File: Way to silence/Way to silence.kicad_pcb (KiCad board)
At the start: 2 copper layers, 62 parts, among them J1 SD Card Connector, J2 Amplificator_Terminal, J3 5V_Terminal, J4 Battery_Terminal, Q1 BC817, Q2 BC817, SW1 SW_SPDT, U1 ESP32-WROOM-32-N16, U2 SM5308, U3 CP2102-GMR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

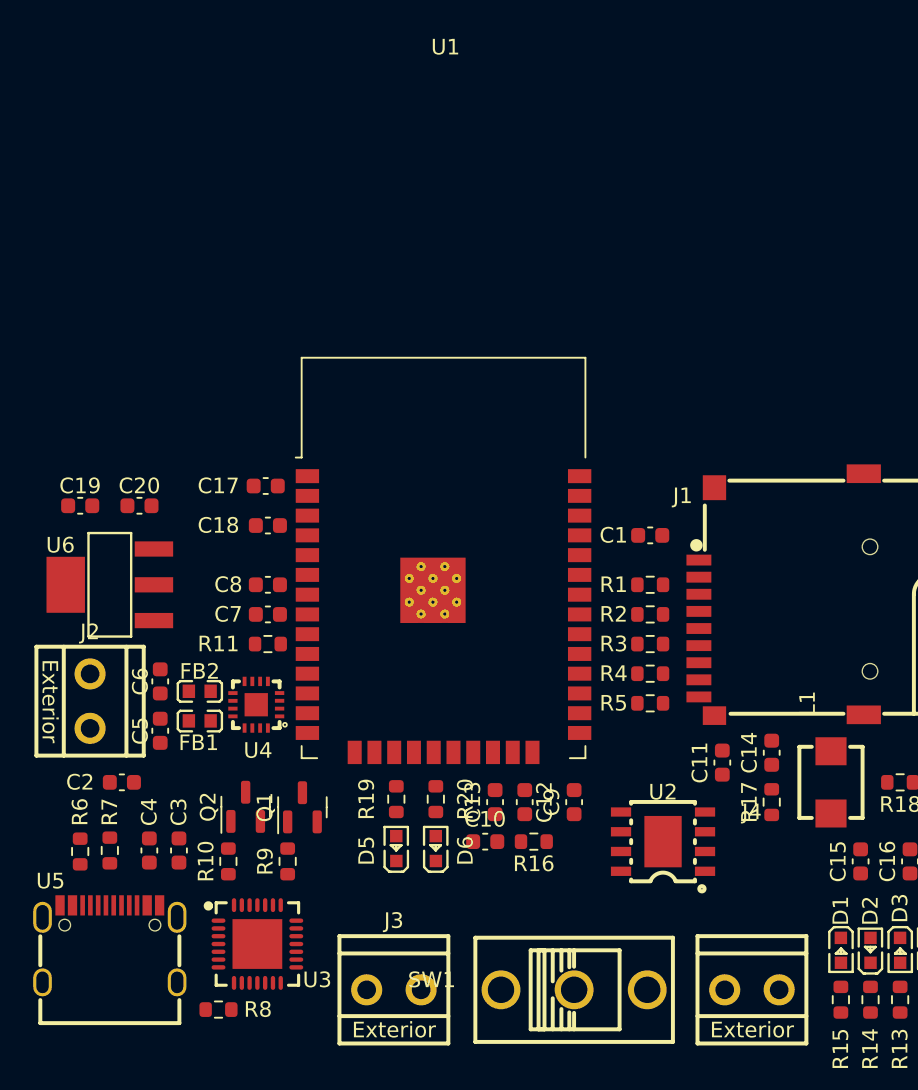
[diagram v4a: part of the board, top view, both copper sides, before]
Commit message: [ADD] Placement adjustements
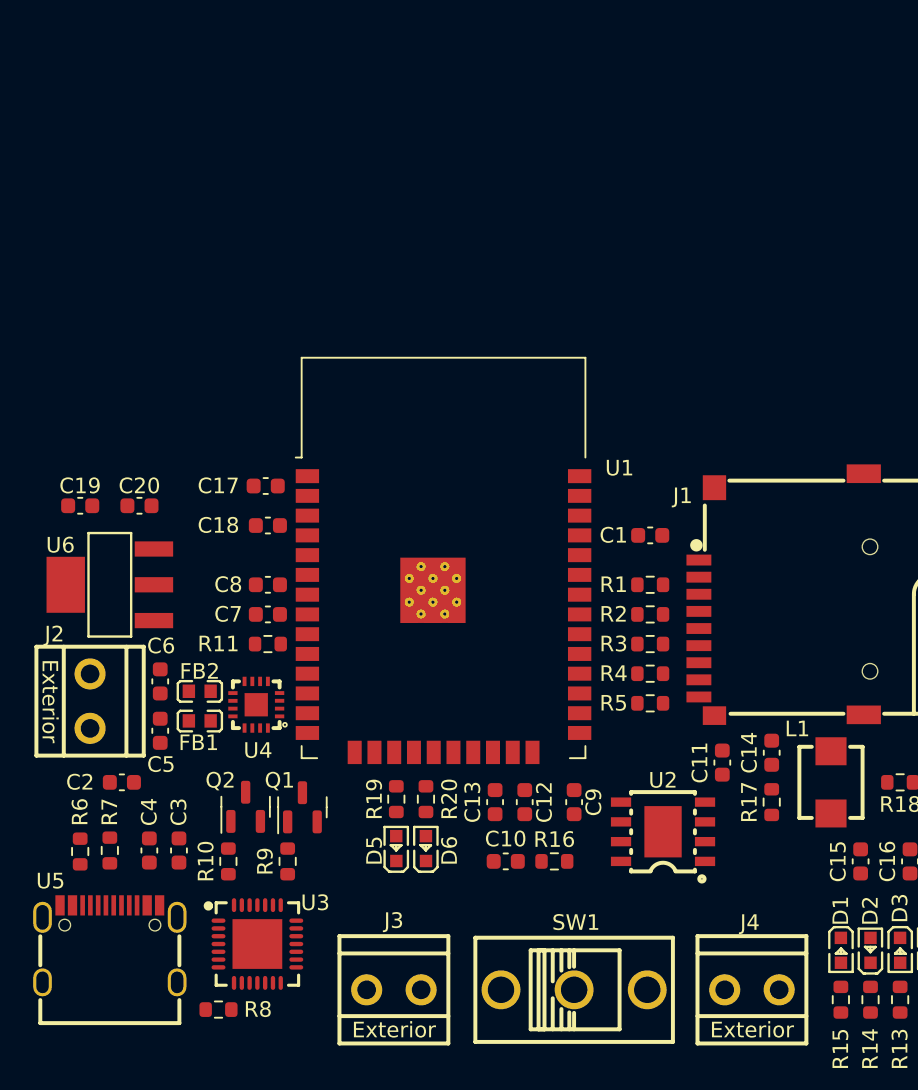
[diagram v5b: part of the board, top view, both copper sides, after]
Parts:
- moved C10 1.83 mm to (94.0, 70.5)
- moved R16 1.83 mm to (97.2, 70.5)
- moved U2 0.64 mm to (104.1, 68.6)
- moved D6 0.63 mm to (88.9, 69.7)
- moved R20 0.63 mm to (88.9, 66.5)
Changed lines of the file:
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@@
     (property "ki_keywords" "screw terminal")
     (attr smd)
-    (fp_text reference "J2" (at -4.445 0 unlocked) (layer "F.SilkS")
+    (fp_text reference "J2" (at -4.305 2.286 unlocked) (layer "F.SilkS")
         (effects (font (size 1 1) (thickness 0.1)))
     )
@@
     (property "ki_keywords" "NPN Transistor")
     (attr smd)
-    (fp_text reference "Q2" (at 0 -2.4 90) (layer "F.SilkS")
+    (fp_text reference "Q2" (at 1.6995 -1.618 180) (layer "F.SilkS")
         (effects (font (size 1 1) (thickness 0.15)))
     )
@@
     (property "ki_keywords" "LED diode")
     (attr smd)
-    (fp_text reference "D5" (at -0.14 -1.905 90 unlocked) (layer "F.SilkS")
+    (fp_text reference "D5" (at -0.14 -1.397 90 unlocked) (layer "F.SilkS")
         (effects (font (size 1 1) (thickness 0.1)))
     )
@@
     (property "ki_keywords" "cap capacitor")
     (attr smd)
-    (fp_text reference "C5" (at 0 -1.27 90) (layer "F.SilkS")
+    (fp_text reference "C5" (at -2.172 0.062 180) (layer "F.SilkS")
         (effects (font (size 1 1) (thickness 0.15)))
     )
@@
     (property "ki_keywords" "switch single-pole double-throw spdt ON-ON")
     (attr smd)
-    (fp_text reference "SW1" (at -9.145 -0.635 unlocked) (layer "F.SilkS")
+    (fp_text reference "SW1" (at 0.127 -4.318 unlocked) (layer "F.SilkS")
         (effects (font (size 1 1) (thickness 0.1)))
     )
@@
   )
   (footprint "Way to silence:R_0603_1608Metric" (layer "F.Cu")
-    (at 89.535 66.485 90)
+    (at 88.9 66.485 90)
     (descr "Resistor SMD 0603 (1608 Metric), square (rectangular) end terminal, IPC_7351 nominal, (Body size source: IPC-SM-782 page 72, https://www.pcb-3d.com/wordpress/wp-content/uploads/ipc-sm-782a_amendment_1_and_2.pdf), generated with kicad-footprint-generator")
     (tags "resistor")
@@
     (property "ki_keywords" "R res resistor")
     (attr smd)
-    (fp_text reference "R20" (at 0 1.905 90) (layer "F.SilkS")
+    (fp_text reference "R20" (at 0 1.524 90) (layer "F.SilkS")
         (effects (font (size 1 1) (thickness 0.15)))
     )
-    (fp_text value "1K" (at 0 1.43 90) (layer "F.Fab")
+    (fp_text value "1K" (at 0 1.27 90) (layer "F.Fab")
         (effects (font (size 1 1) (thickness 0.15)))
     )
@@
     (property "Sheetname" "")
     (attr smd)
-    (fp_text reference "U1" (at 0 -35.56 unlocked) (layer "F.SilkS")
+    (fp_text reference "U1" (at 11.186 -8.498 unlocked) (layer "F.SilkS")
         (effects (font (size 1 1) (thickness 0.1)))
     )
@@
     (property "ki_keywords" "R res resistor")
     (attr smd)
-    (fp_text reference "R19" (at 0 -1.905 90) (layer "F.SilkS")
+    (fp_text reference "R19" (at 0 -1.397 90) (layer "F.SilkS")
         (effects (font (size 1 1) (thickness 0.15)))
     )
@@
     (property "Sheetname" "USB to Uart")
     (attr smd)
-    (fp_text reference "U3" (at 2.309 -3.85 unlocked) (layer "F.SilkS")
+    (fp_text reference "U3" (at -2.644 -3.723 unlocked) (layer "F.SilkS")
         (effects (font (size 1 1) (thickness 0.1)))
     )
@@
   )
   (footprint "Way to silence:SM5308" (layer "F.Cu")
-    (at 104.14 69.215 180)
+    (at 104.14 68.58 180)
     (property "LCSC" "C5345582")
     (property "Sheetfile" "battery_management.kicad_sch")
     (property "Sheetname" "Battery Management")
     (attr smd)
-    (fp_text reference "U2" (at 0 3.175 unlocked) (layer "F.SilkS")
+    (fp_text reference "U2" (at 0 3.302 unlocked) (layer "F.SilkS")
         (effects (font (size 1 1) (thickness 0.1)))
     )
@@
   )
   (footprint "Way to silence:R_0603_1608Metric" (layer "F.Cu")
-    (at 95.835 69.215 180)
+    (at 97.155 70.485 180)
     (descr "Resistor SMD 0603 (1608 Metric), square (rectangular) end terminal, IPC_7351 nominal, (Body size source: IPC-SM-782 page 72, https://www.pcb-3d.com/wordpress/wp-content/uploads/ipc-sm-782a_amendment_1_and_2.pdf), generated with kicad-footprint-generator")
     (tags "resistor")
@@
     (property "ki_keywords" "R res resistor")
     (attr smd)
-    (fp_text reference "R16" (at 0 -1.43) (layer "F.SilkS")
+    (fp_text reference "R16" (at 0 1.397) (layer "F.SilkS")
         (effects (font (size 1 1) (thickness 0.15)))
     )
@@
     (property "ki_keywords" "inductor choke coil reactor magnetic")
     (attr smd)
-    (fp_text reference "L1" (at 5.08 -1.5 90 unlocked) (layer "F.SilkS")
+    (fp_text reference "L1" (at 3.429 -2.159 unlocked) (layer "F.SilkS")
         (effects (font (size 1 1) (thickness 0.1)))
     )
@@
   )
   (footprint "Way to silence:LED_0603" (layer "F.Cu")
-    (at 89.535 69.66 90)
+    (at 88.9 69.66 90)
     (property "LCSC" "C84263")
     (property "Sheetfile" "Way to silence.kicad_sch")
@@
     (property "ki_keywords" "LED diode")
     (attr smd)
-    (fp_text reference "D6" (at -0.14 1.905 90 unlocked) (layer "F.SilkS")
+    (fp_text reference "D6" (at -0.14 1.524 90 unlocked) (layer "F.SilkS")
         (effects (font (size 1 1) (thickness 0.1)))
     )
@@
   )
   (footprint "Way to silence:C_0603_1608Metric" (layer "F.Cu")
-    (at 92.71 69.215)
+    (at 94.03 70.485)
     (descr "Capacitor SMD 0603 (1608 Metric), square (rectangular) end terminal, IPC_7351 nominal, (Body size source: IPC-SM-782 page 76, https://www.pcb-3d.com/wordpress/wp-content/uploads/ipc-sm-782a_amendment_1_and_2.pdf), generated with kicad-footprint-generator")
     (tags "capacitor")
@@
     (property "ki_keywords" "cap capacitor")
     (attr smd)
-    (fp_text reference "C9" (at 0 -1.43 90) (layer "F.SilkS")
+    (fp_text reference "C9" (at 0 1.27 90) (layer "F.SilkS")
         (effects (font (size 1 1) (thickness 0.15)))
     )
@@
     (property "ki_keywords" "cap capacitor")
     (attr smd)
-    (fp_text reference "C6" (at 0 1.27 90) (layer "F.SilkS")
+    (fp_text reference "C6" (at -2.273 -0.062 -180) (layer "F.SilkS")
         (effects (font (size 1 1) (thickness 0.15)))
     )
@@
     (property "ki_keywords" "screw terminal")
     (attr smd)
-    (fp_text reference "J4" (at 0 -11.43 unlocked) (layer "F.SilkS")
+    (fp_text reference "J4" (at -0.127 -4.318 unlocked) (layer "F.SilkS")
         (effects (font (size 1 1) (thickness 0.1)))
     )
@@
     (property "ki_keywords" "NPN Transistor")
     (attr smd)
-    (fp_text reference "Q1" (at 0 -2.4 90) (layer "F.SilkS")
+    (fp_text reference "Q1" (at 1.7295 -1.458 180) (layer "F.SilkS")
         (effects (font (size 1 1) (thickness 0.15)))
     )

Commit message: [ADD] 3d Models
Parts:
- moved C6 3.55 mm to (73.7, 55.9)
- moved C5 3.24 mm to (73.7, 64.8)
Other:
- board text added: "5V IN"
- board text added: "Battery"
- board text added: "POWER MODE"
- board text added: "Speaker"
- board text added: "VIN"
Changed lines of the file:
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@@
         (effects (font (size 1 1) (thickness 0.15)))
     )
+    (fp_text user "-" (at 0.762 -3.81 -90 unlocked) (layer "F.SilkS")
+        (effects (font (size 2 2) (thickness 0.2)) (justify left bottom))
+    )
     (fp_text user "Exterior" (at 0 3.175 -90 unlocked) (layer "F.SilkS")
         (effects (font (size 1 1) (thickness 0.1)) (justify bottom))
     )
+    (fp_text user "+" (at -3.302 -3.81 -90 unlocked) (layer "F.SilkS")
+        (effects (font (size 2 2) (thickness 0.2)) (justify left bottom))
+    )
     (fp_text user "gge106" (at 0 0 90) (layer "Cmts.User")
         (effects (font (size 1 1) (thickness 0.15)))
@@
     (pad "2" smd rect (at 0.8 -0.003) (size 0.8 0.8) (layers "F.Cu" "F.Paste" "F.Mask")
       (net 14 "Net-(D1-A)") (pinfunction "A") (pintype "passive"))
+    (model ":KICAD7_3DMODEL_DIR:LED_SMD.3dshapes/LED_0603_1608Metric.step"
+      (offset (xyz 0 0 0))
+      (scale (xyz 1 1 1))
+      (rotate (xyz 0 0 0))
+    )
   )
   (footprint "Package_TO_SOT_SMD:SOT-23" (layer "F.Cu")
@@
     (pad "2" smd rect (at 0.8 -0.003 180) (size 0.8 0.8) (layers "F.Cu" "F.Paste" "F.Mask")
       (net 18 "Net-(D5-A)") (pinfunction "A") (pintype "passive"))
+    (model ":KICAD7_3DMODEL_DIR:LED_SMD.3dshapes/LED_0603_1608Metric.step"
+      (offset (xyz 0 0 0))
+      (scale (xyz 1 1 1))
+      (rotate (xyz 0 0 0))
+    )
   )
   (footprint "Way to silence:C_0603_1608Metric" (layer "F.Cu")
-    (at 71.82 62.09 90)
+    (at 73.66 64.757 90)
     (descr "Capacitor SMD 0603 (1608 Metric), square (rectangular) end terminal, IPC_7351 nominal, (Body size source: IPC-SM-782 page 76, https://www.pcb-3d.com/wordpress/wp-content/uploads/ipc-sm-782a_amendment_1_and_2.pdf), generated with kicad-footprint-generator")
     (tags "capacitor")
@@
     (property "ki_keywords" "cap capacitor")
     (attr smd)
-    (fp_text reference "C5" (at -2.172 0.062 180) (layer "F.SilkS")
+    (fp_text reference "C5" (at -0.013 -1.524 180) (layer "F.SilkS")
         (effects (font (size 1 1) (thickness 0.15)))
     )
@@
     (pad "2" smd rect (at 0.7 0) (size 0.8 0.864) (layers "F.Cu" "F.Paste" "F.Mask")
       (net 5 "Net-(J2-Pin_2)") (pintype "passive"))
+    (model ":KICAD7_3DMODEL_DIR:Capacitor_SMD.3dshapes/C_0603_1608Metric.step"
+      (offset (xyz 0 0 0))
+      (scale (xyz 1 1 1))
+      (rotate (xyz 0 0 0))
+    )
   )
   (footprint "Way to silence:R_0603_1608Metric" (layer "F.Cu")
@@
     (pad "2" smd rect (at 0.8 -0.003 180) (size 0.8 0.8) (layers "F.Cu" "F.Paste" "F.Mask")
       (net 13 "Net-(D1-K)") (pinfunction "A") (pintype "passive"))
+    (model ":KICAD7_3DMODEL_DIR:LED_SMD.3dshapes/LED_0603_1608Metric.step"
+      (offset (xyz 0 0 0))
+      (scale (xyz 1 1 1))
+      (rotate (xyz 0 0 0))
+    )
   )
   (footprint "Way to silence:C_0603_1608Metric" (layer "F.Cu")
@@
     (property "ki_keywords" "switch single-pole double-throw spdt ON-ON")
     (attr smd)
-    (fp_text reference "SW1" (at 0.127 -4.318 unlocked) (layer "F.SilkS")
+    (fp_text reference "SW1" (at -0.635 -4.318 unlocked) (layer "F.SilkS")
         (effects (font (size 1 1) (thickness 0.1)))
     )
@@
     (pad "3" thru_hole circle (at 4.7 0) (size 2.5 2.5) (drill 1.7) (layers "*.Cu" "*.Paste" "*.Mask")
       (net 9 "/Battery Management/VOUT") (pinfunction "C") (pintype "passive"))
+    (model ":KICAD7_3DMODEL_DIR:Button_Switch_THT.3dshapes/SW_CuK_JS202011CQN_DPDT_Straight.step"
+      (offset (xyz -3.5 2.75 0))
+      (scale (xyz 1.4 1.7 1))
+      (rotate (xyz 0 0 0))
+    )
   )
   (footprint "Way to silence:LED_0603" (layer "F.Cu")
@@
     (pad "2" smd rect (at 0.8 -0.003 180) (size 0.8 0.8) (layers "F.Cu" "F.Paste" "F.Mask")
       (net 13 "Net-(D1-K)") (pinfunction "A") (pintype "passive"))
+    (model ":KICAD7_3DMODEL_DIR:LED_SMD.3dshapes/LED_0603_1608Metric.step"
+      (offset (xyz 0 0 0))
+      (scale (xyz 1 1 1))
+      (rotate (xyz 0 0 0))
+    )
   )
   (footprint "Way to silence:AMS1117CD-3.3" (layer "F.Cu")
@@
     (fp_line (start 3.326 1.371) (end -3.326 1.371)
       (stroke (width 0.152) (type solid)) (layer "F.SilkS"))
-    (fp_circle (center -2.413 3.556) (end -2.413 3.806)
-      (stroke (width 0.5) (type solid)) (fill none) (layer "Cmts.User"))
     (pad "1" smd rect (at -2.3 2.835) (size 2.47 0.98) (layers "F.Cu" "F.Paste" "F.Mask")
       (net 2 "GND") (pinfunction "GND") (pintype "power_in"))
@@
     (pad "4" smd rect (at 0 -2.835) (size 2.47 3.6) (layers "F.Cu" "F.Paste" "F.Mask")
       (net 98 "unconnected-(U6-Tab-Pad4)") (pinfunction "Tab") (pintype "no_connect"))
+    (model ":KICAD7_3DMODEL_DIR:Package_TO_SOT_SMD.3dshapes/SOT-223.step"
+      (offset (xyz 0 0 0))
+      (scale (xyz 1 1 1))
+      (rotate (xyz 0 0 -90))
+    )
   )
   (footprint "Way to silence:R_0603_1608Metric" (layer "F.Cu")
@@
         (effects (font (size 1 1) (thickness 0.15)))
     )
-    (fp_text user "KEEP-OUT ZONE" (at -0.08 -22.22) (layer "Cmts.User")
-        (effects (font (size 2 2) (thickness 0.15)))
-    )
     (fp_text user "Antenna" (at -0.13 -12.74) (layer "Cmts.User")
         (effects (font (size 1 1) (thickness 0.15)))
     )
+    (fp_text user "KEEP-OUT ZONE" (at -0.08 -22.22) (layer "Cmts.User")
+        (effects (font (size 2 2) (thickness 0.15)))
+    )
     (fp_text user "${REFERENCE}" (at 0 -32.56 unlocked) (layer "F.Fab")
         (effects (font (size 1 1) (thickness 0.15)))
@@
     (pad "2" smd rect (at 2 0 180) (size 2 1.8) (layers "F.Cu" "F.Paste" "F.Mask")
       (net 11 "/Battery Management/BAT") (pinfunction "2") (pintype "passive"))
+    (model ":KICAD7_3DMODEL_DIR:Inductor_SMD.3dshapes/L_Bourns_SRP2313AA.step"
+      (offset (xyz 0 0 0))
+      (scale (xyz 0.2 0.2 0.2))
+      (rotate (xyz 0 0 0))
+    )
   )
   (footprint "Way to silence:LED_0603" (layer "F.Cu")
@@
     (pad "2" smd rect (at 0.8 -0.003) (size 0.8 0.8) (layers "F.Cu" "F.Paste" "F.Mask")
       (net 16 "Net-(D3-A)") (pinfunction "A") (pintype "passive"))
+    (model ":KICAD7_3DMODEL_DIR:LED_SMD.3dshapes/LED_0603_1608Metric.step"
+      (offset (xyz 0 0 0))
+      (scale (xyz 1 1 1))
+      (rotate (xyz 0 0 0))
+    )
   )
   (footprint "Way to silence:LED_0603" (layer "F.Cu")
@@
     (pad "2" smd rect (at 0.8 -0.003 180) (size 0.8 0.8) (layers "F.Cu" "F.Paste" "F.Mask")
       (net 19 "Net-(D6-A)") (pinfunction "A") (pintype "passive"))
+    (model ":KICAD7_3DMODEL_DIR:LED_SMD.3dshapes/LED_0603_1608Metric.step"
+      (offset (xyz 0 0 0))
+      (scale (xyz 1 1 1))
+      (rotate (xyz 0 0 0))
+    )
   )
   (footprint "Way to silence:C_0603_1608Metric" (layer "F.Cu")
@@
         (effects (font (size 1 1) (thickness 0.15)))
     )
+    (fp_text user "-" (at 0.762 -3.81 unlocked) (layer "F.SilkS")
+        (effects (font (size 2 2) (thickness 0.2)) (justify left bottom))
+    )
+    (fp_text user "+" (at -3.302 -3.81 unlocked) (layer "F.SilkS")
+        (effects (font (size 2 2) (thickness 0.2)) (justify left bottom))
+    )
     (fp_text user "Exterior" (at 0 3.175 unlocked) (layer "F.SilkS")
         (effects (font (size 1 1) (thickness 0.1)) (justify bottom))
@@
   )
   (footprint "Way to silence:C_0603_1608Metric" (layer "F.Cu")
-    (at 71.82 58.915 -90)
+    (at 73.66 55.88 -90)
     (descr "Capacitor SMD 0603 (1608 Metric), square (rectangular) end terminal, IPC_7351 nominal, (Body size source: IPC-SM-782 page 76, https://www.pcb-3d.com/wordpress/wp-content/uploads/ipc-sm-782a_amendment_1_and_2.pdf), generated with kicad-footprint-generator")
     (tags "capacitor")
@@
         (effects (font (size 1 1) (thickness 0.15)))
     )
+    (fp_text user "+" (at -3.302 -3.81 unlocked) (layer "F.SilkS")
+        (effects (font (size 2 2) (thickness 0.2)) (justify left bottom))
+    )
     (fp_text user "Exterior" (at 0 3.175 unlocked) (layer "F.SilkS")
         (effects (font (size 1 1) (thickness 0.1)) (justify bottom))
     )
+    (fp_text user "-" (at 0.762 -3.81 unlocked) (layer "F.SilkS")
+        (effects (font (size 2 2) (thickness 0.2)) (justify left bottom))
+    )
     (fp_text user "gge106" (at 0 0) (layer "Cmts.User")
         (effects (font (size 1 1) (thickness 0.15)))
@@
     (property "ki_keywords" "L ferrite bead inductor filter")
     (attr smd)
-    (fp_text reference "FB2" (at 0 1.27 unlocked) (layer "F.SilkS")
+    (fp_text reference "FB2" (at 0 1.384 unlocked) (layer "F.SilkS")
         (effects (font (size 1 1) (thickness 0.1)))
     )
@@
     (pad "2" smd rect (at 0.7 0) (size 0.8 0.864) (layers "F.Cu" "F.Paste" "F.Mask")
       (net 6 "Net-(J2-Pin_1)") (pintype "passive"))
+    (model ":KICAD7_3DMODEL_DIR:Capacitor_SMD.3dshapes/C_0603_1608Metric.step"
+      (offset (xyz 0 0 0))
+      (scale (xyz 1 1 1))
+      (rotate (xyz 0 0 0))
+    )
   )
   (footprint "Way to silence:C_0603_1608Metric" (layer "F.Cu")
@@
       (net 2 "GND") (pinfunction "SHIELD") (pintype "passive"))
     (model ":KICAD7_3DMODEL_DIR:Connector_Card.3dshapes/microSD_HC_Hirose_DM3D-SF.step"
-      (offset (xyz -3.4 0 0))
-      (scale (xyz 1 1 1))
+      (offset (xyz 0 -2.5 0))
+      (scale (xyz 1.3 1.3 1))
       (rotate (xyz 0 0 180))
     )
@@
     )
   )
+  (gr_text "VIN" (at 91.948 74.93) (layer "F.SilkS")
+    (effects (font (size 1 1) (thickness 0.2) bold) (justify left bottom))
+  )
+  (gr_text "Battery" (at 100.076 74.93) (layer "F.SilkS")
+    (effects (font (size 1 1) (thickness 0.2) bold) (justify left bottom))
+  )
+  (gr_text "Battery" (at 107.442 72.898) (layer "F.SilkS")
+    (effects (font (size 1 1) (thickness 0.2) bold) (justify left bottom))
+  )
+  (gr_text "Speaker" (at 64.262 64.008 -90) (layer "F.SilkS")
+    (effects (font (size 1 1) (thickness 0.2) bold) (justify left bottom))
+  )
+  (gr_text "POWER MODE" (at 92.71 73.406) (layer "F.SilkS")
+    (effects (font (size 1.2 1.2) (thickness 0.2) bold) (justify left bottom))
+  )
+  (gr_text "5V IN" (at 84.836 72.898) (layer "F.SilkS")
+    (effects (font (size 1 1) (thickness 0.2) bold) (justify left bottom))
+  )
 )

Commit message: [ADD] Board Shape ok
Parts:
- moved C11 2.79 mm to (105.4, 63.0)
- moved D1 2.54 mm to (114.6, 73.9)
- moved D2 2.54 mm to (116.5, 73.9)
- moved D3 2.54 mm to (118.4, 73.9)
- moved D4 2.54 mm to (120.3, 73.9)
- moved R12 2.54 mm to (120.3, 77.1)
- moved R13 2.54 mm to (118.4, 77.1)
- moved R14 2.54 mm to (116.5, 77.1)
- moved R15 2.54 mm to (114.6, 77.1)
- moved C15 2.39 mm to (117.9, 68.3)
- moved C16 2.25 mm to (120.7, 68.3)
- moved R8 1.97 mm to (77.5, 80.5)
- moved L1 1.66 mm to (113.3, 65.5)
- moved U5 1.59 mm to (69.3, 77.2)
- moved R18 1.17 mm to (119.1, 64.3)
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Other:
- board outline added: 57.9 x 38.1 mm
- board text added: "Way To Silence"
